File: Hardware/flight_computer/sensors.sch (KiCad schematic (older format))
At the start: 14 parts, among them U10 CAM-M8Q-0, U11 BMI088, U12 LIS3MDLTR, U13 Barometer

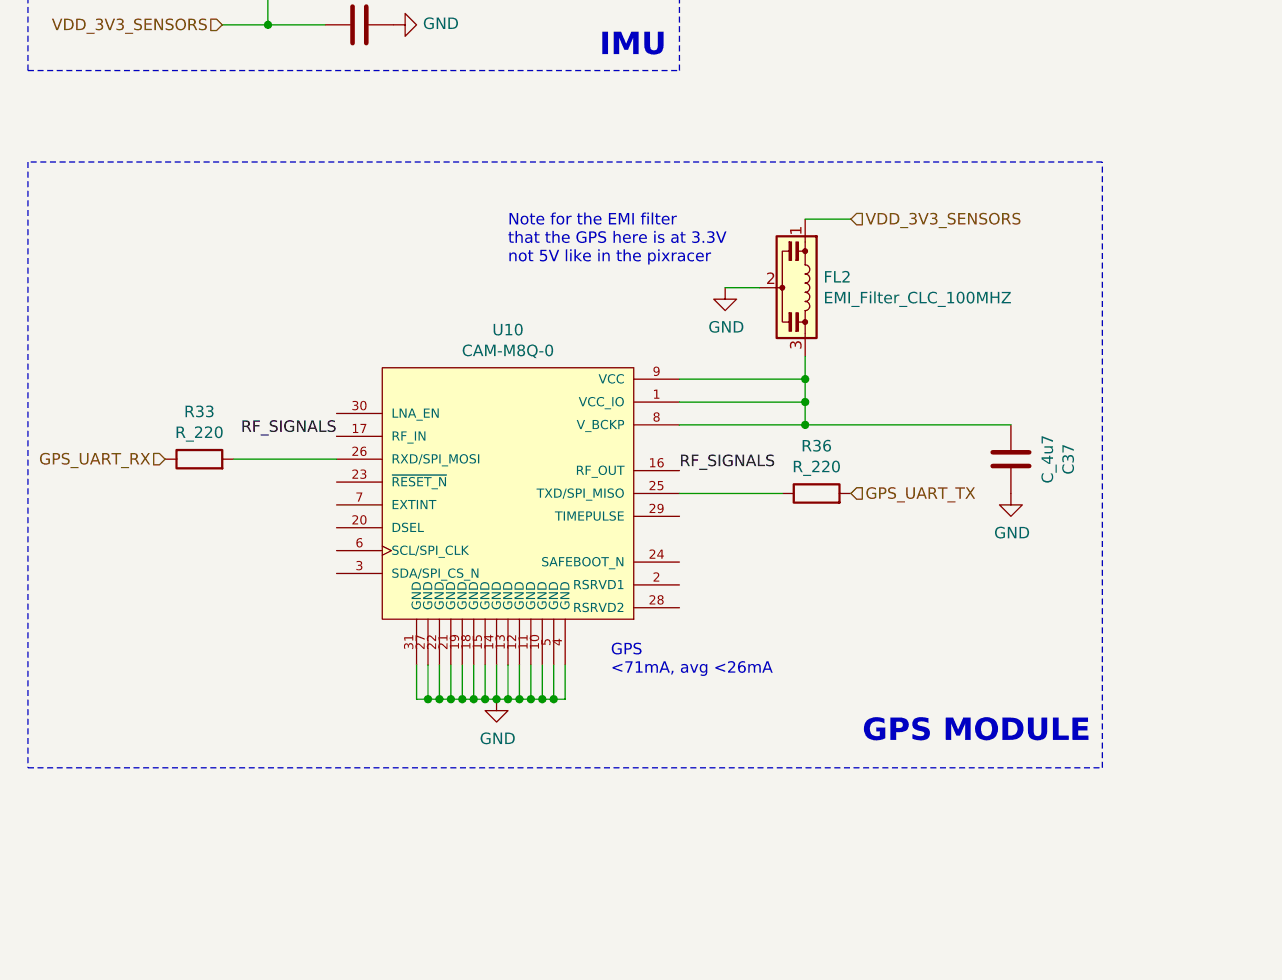
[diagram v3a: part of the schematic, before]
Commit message: added wider dxf, updated footrprints to show 3D models, adde new dxf to layout and kept old as a dwg in a last ditch attempt to keep the board smaller.
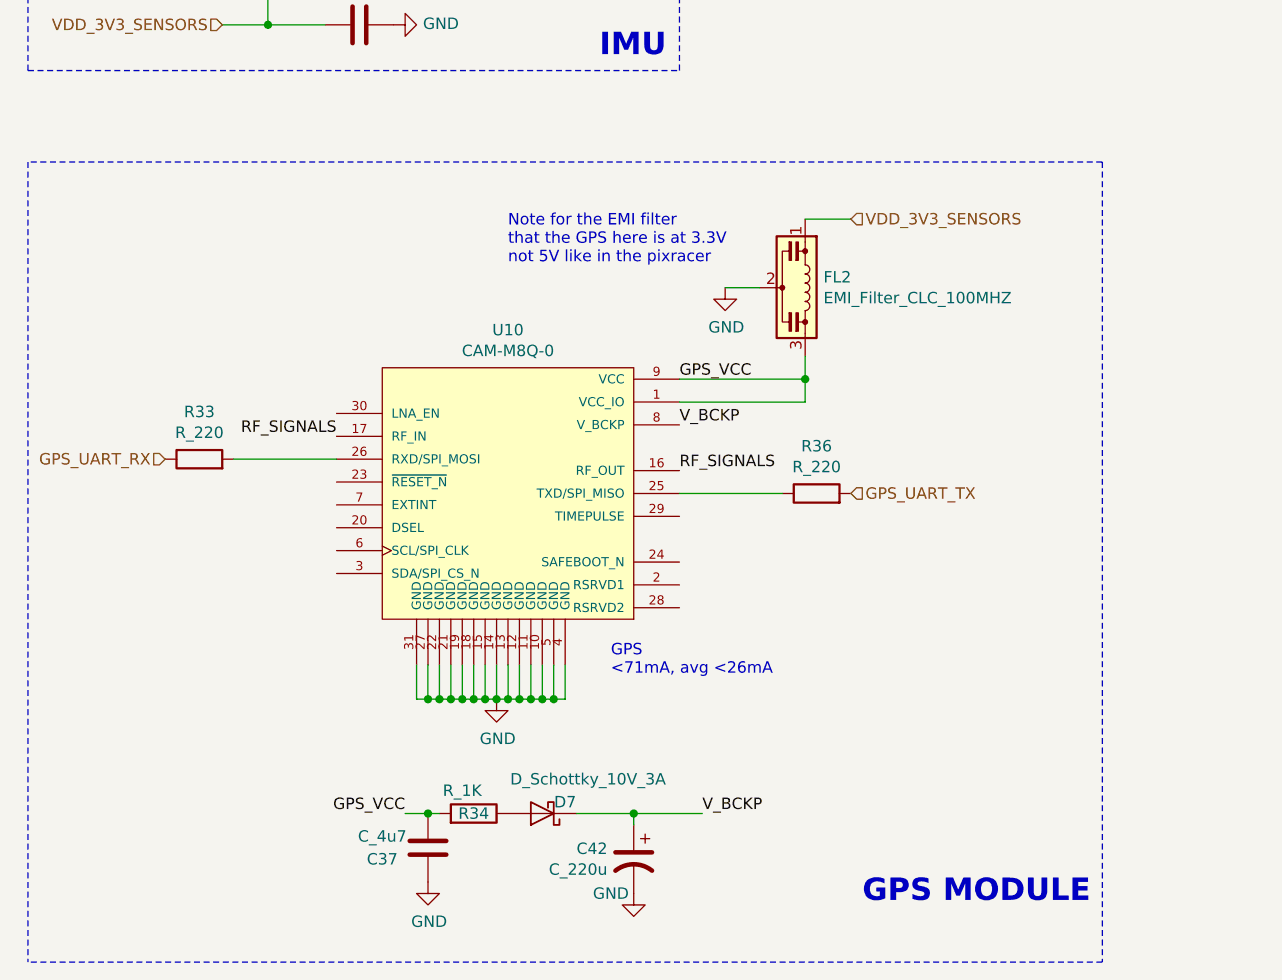
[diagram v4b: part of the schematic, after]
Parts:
- added C42: C_220u, drone_footprints:UWT0G221MCL6GS, symbol openDrone_parts:C_220u
- added D7: D_Schottky_10V_3A, Diodes_SMD:D_SOD-323F, symbol openDrone_parts:D_Schottky_10V_3A
- added R34: R_1K, Resistors_SMD:R_0805, symbol openDrone_parts:R_1K
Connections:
- net GND: now also C42.2
- net GPS_VCC: now reaches C37.2, FL2.3, U10.1 (VCC_IO), U10.9 (VCC)
- net GPS_VCC: now also R34.2; no longer U10.8 (V_BCKP)
- new net: D7.2 (A), R34.1
- new net V_BCKP: C42.1, D7.1 (K), U10.8 (V_BCKP)
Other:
- moved on the sheet: C37
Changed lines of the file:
@@
 	4300 4200 4300 4100
 Connection ~ 4300 4100
-Wire Wire Line
-	3750 4300 4300 4300
-Wire Wire Line
-	4300 4300 4300 4200
-Connection ~ 4300 4200
 $Comp
 L openDrone_parts:C_4u7 C37
 U 1 1 5F87B412
-P 5200 4450
-F 0 "C37" V 4948 4450 50  0000 C CNN
-F 1 "C_4u7" V 5039 4450 50  0000 C CNN
-F 2 "Capacitors_SMD:C_0805" H 5238 4300 50  0001 C CNN
-F 3 "" H 5225 4550 50  0001 C CNN
-F 4 "490-14466-1-ND" H 5200 4450 60  0001 C CNN "DPN"
-	1    5200 4450
+P 2650 6150
+F 0 "C37" H 2850 6200 50  0000 C CNN
+F 1 "C_4u7" H 2850 6100 50  0000 C CNN
+F 2 "Capacitors_SMD:C_0805" H 2688 6000 50  0001 C CNN
+F 3 "" H 2675 6250 50  0001 C CNN
+F 4 "490-14466-1-ND" H 2650 6150 60  0001 C CNN "DPN"
+	1    2650 6150
 	-1   0    0    1
 $EndComp
-Wire Wire Line
-	5200 4300 4300 4300
-Connection ~ 4300 4300
 Text Notes 8650 2000 0    50   ~ 0
 Magnetometer\n40-270uA
@@
 L power:GND #PWR053
 U 1 1 5FB16EE2
-P 5200 4600
-F 0 "#PWR053" H 5200 4350 50  0001 C CNN
-F 1 "GND" H 5205 4427 50  0000 C CNN
-F 2 "" H 5200 4600 50  0001 C CNN
-F 3 "" H 5200 4600 50  0001 C CNN
-	1    5200 4600
+P 2650 6300
+F 0 "#PWR053" H 2650 6050 50  0001 C CNN
+F 1 "GND" H 2655 6127 50  0000 C CNN
+F 2 "" H 2650 6300 50  0001 C CNN
+F 3 "" H 2650 6300 50  0001 C CNN
+	1    2650 6300
 	1    0    0    -1
 $EndComp
@@
 VDD_3V3_SENSORS
 Wire Notes Line
-	900  5800 5600 5800
-Wire Notes Line
-	5600 5800 5600 3150
-Wire Notes Line
 	5600 3150 900  3150
-Wire Notes Line
-	900  3150 900  5800
-Text Notes 4550 5700 0    98   ~ 20
+Text Notes 4550 6400 0    98   ~ 20
 GPS MODULE
 Wire Notes Line
@@
 Text Notes 2800 2450 0    50   ~ 0
 Check VDDIO connection
+$Comp
+L openDrone_parts:R_1K R?
+U 1 1 5F866B0B
+P 2850 6000
+AR Path="/5F866B0B" Ref="R?"  Part="1"
+AR Path="/5F84A65B/5F866B0B" Ref="R?"  Part="1"
+AR Path="/5F5F0393/5F866B0B" Ref="R34"  Part="1"
+F 0 "R34" H 2850 6000 50  0000 C CNN
+F 1 "R_1K" H 2900 6100 50  0000 C CNN
+F 2 "Resistors_SMD:R_0805" H 2050 6150 50  0001 C CNN
+F 3 "" H 2550 6500 50  0001 C CNN
+F 4 "311-1.0KARCT-ND" H 2200 6250 60  0001 C CNN "DPN"
+	1    2850 6000
+	-1   0    0    -1
+$EndComp
+$Comp
+L openDrone_parts:C_220u C?
+U 1 1 5F866B13
+P 3550 6200
+AR Path="/5F866B13" Ref="C?"  Part="1"
+AR Path="/5F84A65B/5F866B13" Ref="C?"  Part="1"
+AR Path="/5F5F0393/5F866B13" Ref="C42"  Part="1"
+F 0 "C42" H 3665 6246 50  0000 L CNN
+F 1 "C_220u" H 3665 6155 50  0000 L CNN
+F 2 "drone_footprints:UWT0G221MCL6GS" H 4300 6500 50  0001 C CNN
+F 3 "~" H 3550 6200 50  0001 C CNN
+F 4 "493-9872-1-ND" H 3950 6400 50  0001 C CNN "DPN"
+F 5 "UWT0G221MCL6GS" H 4050 6300 50  0001 C CNN "MPN"
+	1    3550 6200
+	-1   0    0    -1
+$EndComp
+Wire Wire Line
+	3550 6000 3550 6050
+$Comp
+L power:GND #PWR?
+U 1 1 5F866B1B
+P 3550 6350
+AR Path="/5F866B1B" Ref="#PWR?"  Part="1"
+AR Path="/5F84A65B/5F866B1B" Ref="#PWR?"  Part="1"
+AR Path="/5F5F0393/5F866B1B" Ref="#PWR056"  Part="1"
+F 0 "#PWR056" H 3550 6100 50  0001 C CNN
+F 1 "GND" H 3650 6350 50  0000 C CNN
+F 2 "" H 3550 6350 50  0001 C CNN
+F 3 "" H 3550 6350 50  0001 C CNN
+	1    3550 6350
+	-1   0    0    -1
+$EndComp
+Wire Wire Line
+	3300 6000 3550 6000
+$Comp
+L openDrone_parts:D_Schottky_10V_3A D?
+U 1 1 5F866B26
+P 3150 6000
+AR Path="/5F866B26" Ref="D?"  Part="1"
+AR Path="/5F5F0393/5F866B26" Ref="D7"  Part="1"
+F 0 "D7" H 3050 5950 50  0000 C CNN
+F 1 "D_Schottky_10V_3A" H 2950 5850 50  0000 C CNN
+F 2 "Diodes_SMD:D_SOD-323F" H 3650 6300 50  0001 C CNN
+F 3 "~" H 3150 6000 50  0001 C CNN
+F 4 "1727-3852-1-ND" H 3550 6200 50  0001 C CNN "DPN"
+F 5 "PMEG1030EJ,115" H 3550 6100 50  0001 C CNN "MPN"
+	1    3150 6000
+	-1   0    0    1
+$EndComp
+Text Label 3750 4300 0    50   ~ 0
+V_BCKP
+Text Label 3850 6000 0    50   ~ 0
+V_BCKP
+Wire Wire Line
+	3850 6000 3550 6000
+Connection ~ 3550 6000
+Text Label 3750 4100 0    50   ~ 0
+GPS_VCC
+Text Label 2550 6000 2    50   ~ 0
+GPS_VCC
+Wire Wire Line
+	2550 6000 2650 6000
+Wire Wire Line
+	2650 6000 2700 6000
+Connection ~ 2650 6000
+Wire Notes Line
+	5600 6650 900  6650
+Wire Notes Line
+	5600 3150 5600 6650
+Wire Notes Line
+	900  3150 900  6650
 $EndSCHEMATC

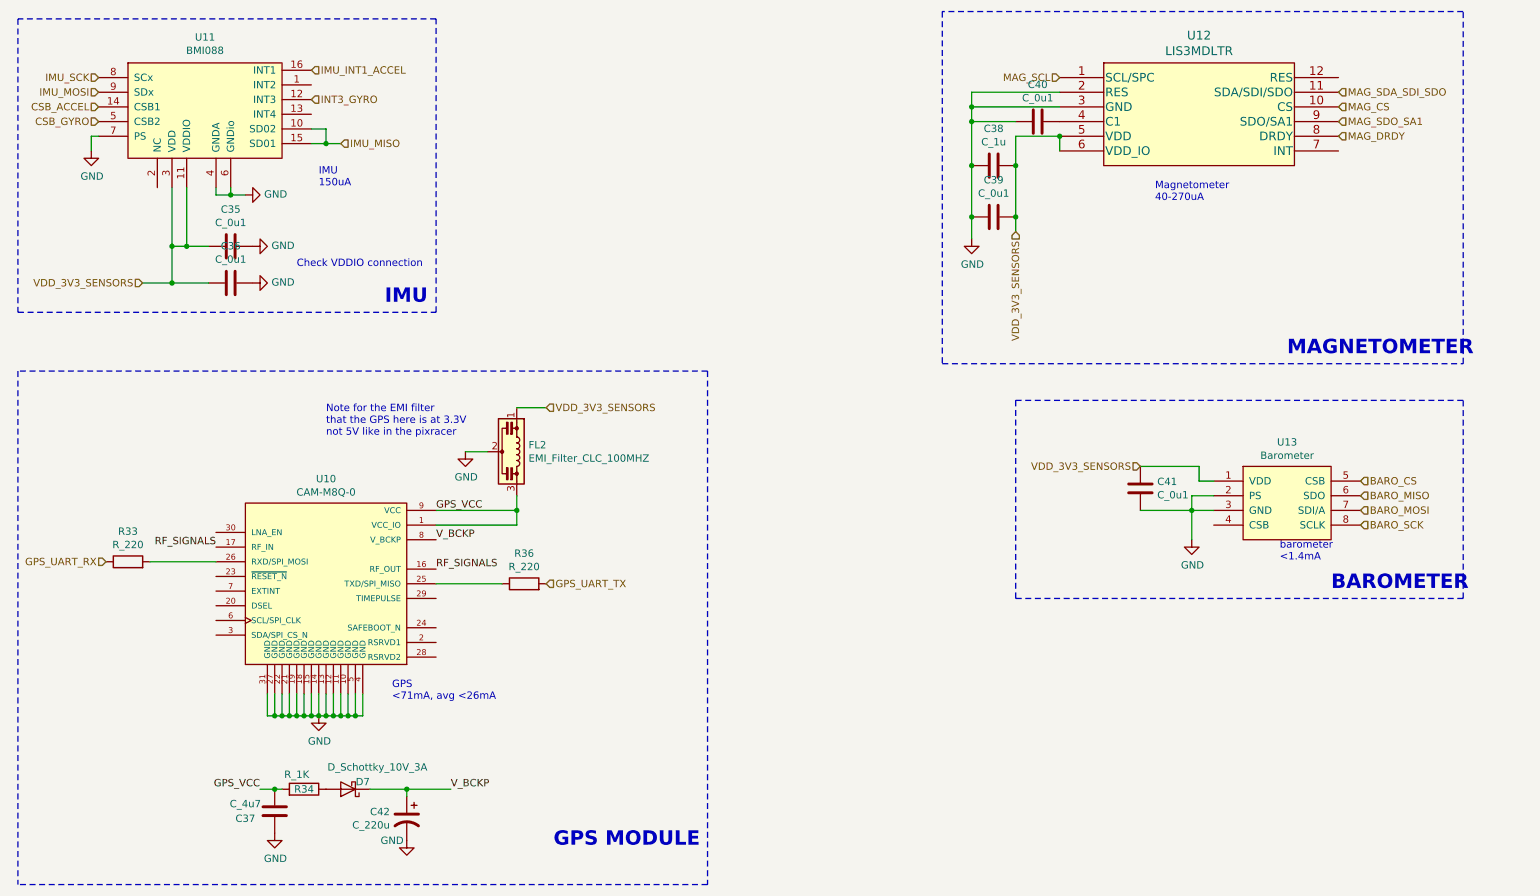
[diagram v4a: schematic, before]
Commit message: added switch components, worked on layout. Sensor 3V3 unfinished.
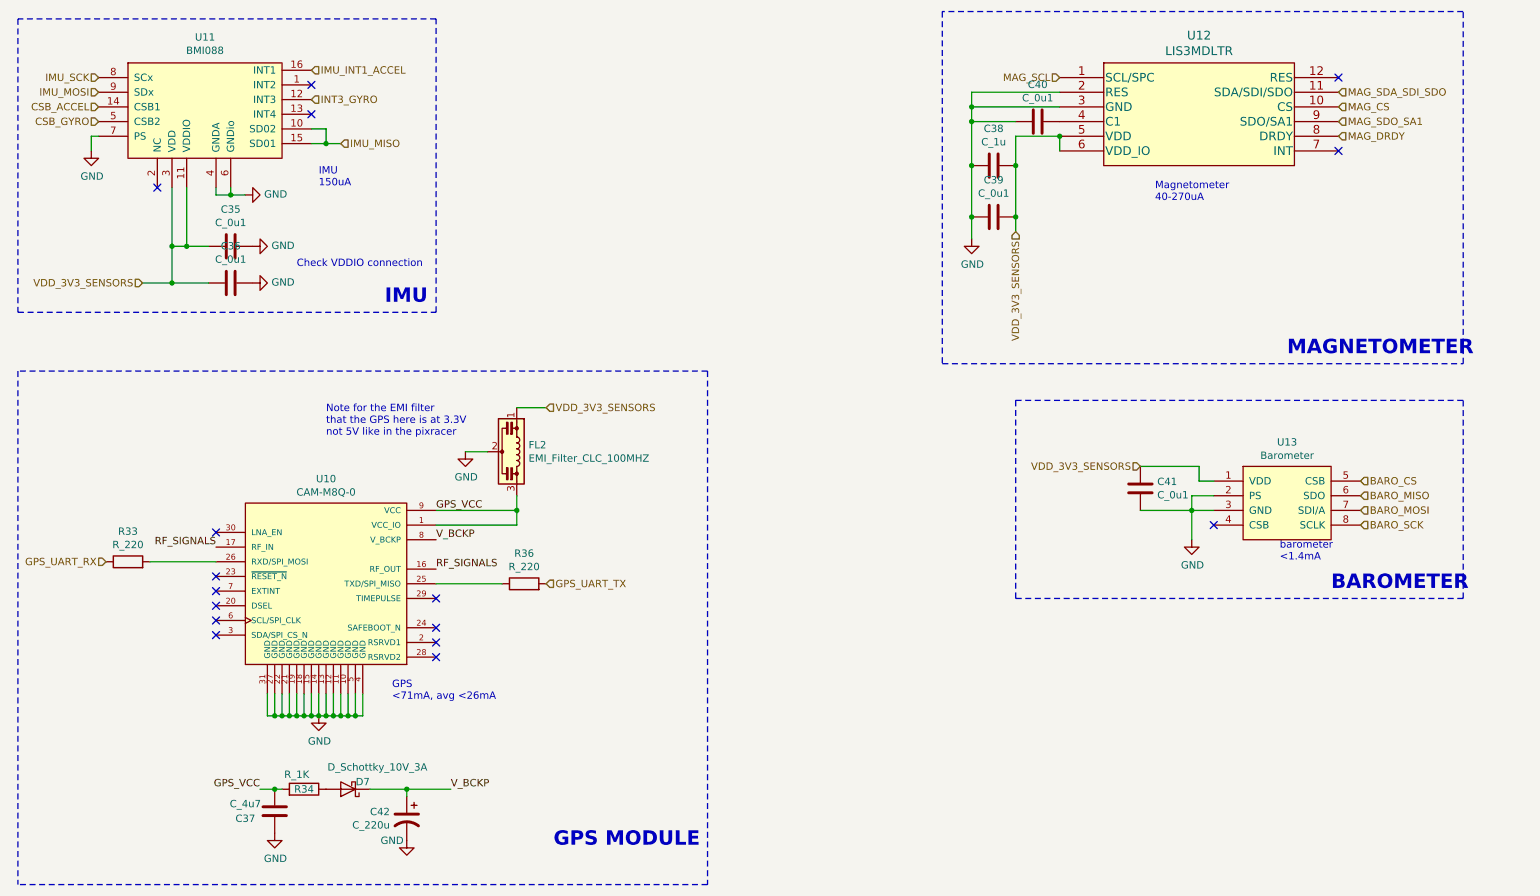
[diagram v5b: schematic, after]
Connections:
- no-connect marks 0 -> 16
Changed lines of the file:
@@
 Wire Notes Line
 	900  3150 900  6650
+NoConn ~ 3750 4900
+NoConn ~ 3750 5000
+NoConn ~ 3750 5100
+NoConn ~ 3750 4700
+NoConn ~ 2250 4250
+NoConn ~ 2250 4550
+NoConn ~ 2250 4650
+NoConn ~ 2250 4750
+NoConn ~ 2250 4850
+NoConn ~ 2250 4950
+NoConn ~ 9900 1150
+NoConn ~ 9900 1650
+NoConn ~ 2900 1400
+NoConn ~ 2900 1200
+NoConn ~ 1850 1900
+NoConn ~ 9050 4200
 $EndSCHEMATC

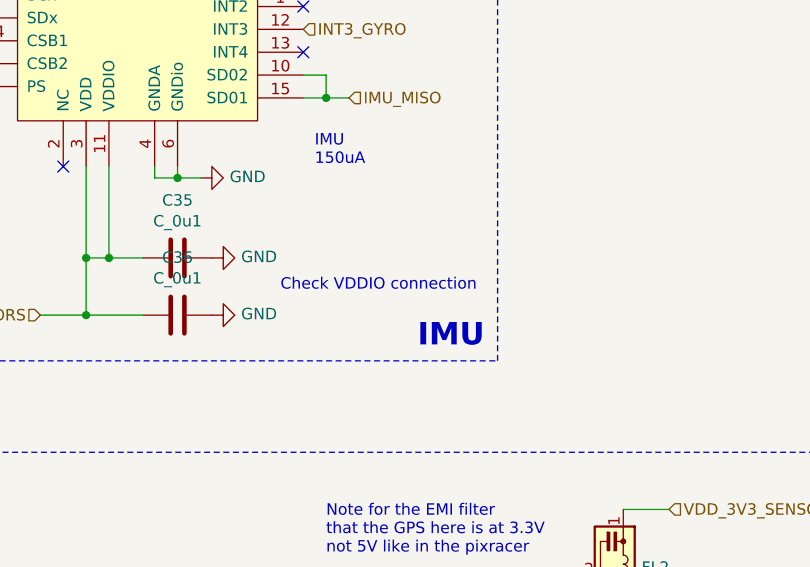
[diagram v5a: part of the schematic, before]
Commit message: fixed issue with RC connector. Try again tomorrow
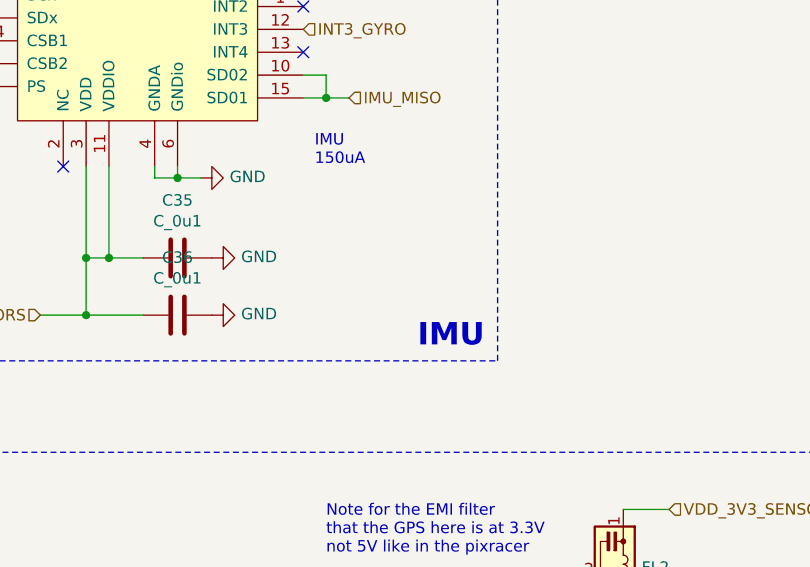
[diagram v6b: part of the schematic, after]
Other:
- note removed: "Check VDDIO connection"
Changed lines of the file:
@@
 Wire Wire Line
 	1950 2300 1950 2550
-Text Notes 2800 2450 0    50   ~ 0
-Check VDDIO connection
 $Comp
 L openDrone_parts:R_1K R?
